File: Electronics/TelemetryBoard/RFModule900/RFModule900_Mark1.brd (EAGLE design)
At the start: 100 x 80 mm, 134 parts, among them T1 DC08-73, T2 DC08-73, U1 TPS2561, U2 TPS2561, U3 LM75B, U4 LTC5505, U5 LTC5505, U6 MCP4728, U7 ADC128D818, U8 MIC5504-3.3YM5, Y1 30 Mhz

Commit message: wiring up new buck and 3.3v ldo
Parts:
- removed JP2, JP3: (no value), SparkFun-Connectors:AVR_ICSP
- added C18, C57, C61: 100uF, SparkFun-Retired:1206
- added C48, C58: 100uF, RitLaunchInitiative:CERAMIC_CAP_1210
- added C59: 47uF, RitLaunchInitiative:CERAMIC_CAP_1210
- added C60, C64, C66: 0.1uF, SparkFun-Capacitors:0402-CAP
- added C62, C63, C65: 1uF, SparkFun-Capacitors:0402-CAP
- added D1, D2: (no value), SparkFun-LED:LED-0603
- added R29: 287, SparkFun-Resistors:0402-RES
- added R30: 90.9k, SparkFun-Resistors:0402-RES
- added R31, R32, R33: 270, SparkFun-Resistors:0402-RES
- added R34, R35: 5k, SparkFun-Resistors:0402-RES
- C32: value 1uF -> DNP
- C54: value 0.1uF -> DNP
- D3: value (none) -> DNP
- R11: value 220 -> DNP
- moved U8 411.2 mm to (12.7, 68.6)
- moved U7 393.7 mm to (31.8, 55.9)
- moved U$15 349.0 mm to (29.2, 8.89)
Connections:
- new net 12V: C48.P$1, C58.P$1, C59.P$1, C60.1, U$15.P$1, U$15.P$11, U$15.P$12, U$15.P$3, U$15.P$39, U$15.P$40
- new net 3V6_PWRGD: U$15.P$8
- new net ADC_INT: U7.6
- new net N$54: R29.2, U$15.P$26
- new net N$55: R30.2, U$15.P$22
- new net N$56: D2.C, R32.2
- new net N$57: R33.2, U8.3
- new net N$58: D1.C, R31.2
- new net N$59: R35.2, U7.8
- new net N$60: R34.2, U7.7
- net 3.3V: now also C63.1, C65.1, C66.1, D2.A, U7.5, U8.5
- net 3.6V: now also C18.1, C57.1, C61.1, C62.2, C64.1, D1.A, R33.1, U$15.P$27, U$15.P$34, U$15.P$35, U$15.P$36, U$15.P$37, U$15.P$38, U$15.P$41, U8.1
- net GND: now also C18.2, C48.P$2, C57.2, C58.P$2, C59.P$2, C60.2, C61.2, C62.1, C63.2, C64.2, C65.2, C66.2, R29.1, R30.1, R31.1, R32.1, R34.1, R35.1, U$15.P$2, U$15.P$20, U$15.P$21, U$15.P$23, U$15.P$31, U$15.P$32, U$15.P$33, U7.4, U8.2
- net SCL: now also U7.3
- net SDA: now also U7.2

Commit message: continued work
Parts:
- added R36, R37, R38: 5k, SparkFun-Resistors:0402-RES
- added R39: DNP, SparkFun-Resistors:0402-RES
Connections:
- new net N$61: R36.2, U3.P$5
- new net N$62: R37.2, U3.P$6
- new net N$63: R38.2, U3.P$7
- new net N$64: R39.2, U6.P$4
- new net PA_OVERTEMP_ALARM: U3.P$3
- net GND: now also R36.1, R37.1, R38.1, R39.1; no longer U6.P$4
- net PA_PWR_REF: now also U7.14
- net PA_PWR_SENSE: now also U7.13
- net PA_TEMP: now also U7.12
- net RF_POWER_IN: now also U7.16
- net RF_POWER_OUT: now also U7.15
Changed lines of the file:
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@@
 <element name="R34" library="SparkFun-Resistors" package="0402-RES" value="5k" x="-95.25" y="-407.67"/>
 <element name="R35" library="SparkFun-Resistors" package="0402-RES" value="5k" x="-95.25" y="-411.48"/>
+<element name="R36" library="SparkFun-Resistors" package="0402-RES" value="5k" x="-95.25" y="-415.29"/>
+<element name="R37" library="SparkFun-Resistors" package="0402-RES" value="5k" x="-95.25" y="-419.1"/>
+<element name="R38" library="SparkFun-Resistors" package="0402-RES" value="5k" x="-95.25" y="-422.91"/>
+<element name="R39" library="SparkFun-Resistors" package="0402-RES" value="DNP" x="-95.25" y="-426.72"/>
 </elements>
 <signals>
@@
 <contactref element="C49" pad="C"/>
 <contactref element="C50" pad="C"/>
-<contactref element="U6" pad="P$4"/>
 <contactref element="C11" pad="2"/>
 <contactref element="C17" pad="1"/>
@@
 <contactref element="R34" pad="1"/>
 <contactref element="R35" pad="1"/>
+<contactref element="R36" pad="1"/>
+<contactref element="R37" pad="1"/>
+<contactref element="R38" pad="1"/>
+<contactref element="R39" pad="1"/>
 <wire x1="-95.83" y1="-407.67" x2="-95.83" y2="-411.48" width="0" layer="19" extent="1-1"/>
+<wire x1="-95.83" y1="-415.29" x2="-95.83" y2="-411.48" width="0" layer="19" extent="1-1"/>
+<wire x1="-95.83" y1="-419.1" x2="-95.83" y2="-415.29" width="0" layer="19" extent="1-1"/>
+<wire x1="-95.83" y1="-422.91" x2="-95.83" y2="-419.1" width="0" layer="19" extent="1-1"/>
+<wire x1="-95.83" y1="-426.72" x2="-95.83" y2="-422.91" width="0" layer="19" extent="1-1"/>
 <wire x1="-94.67" y1="-403.86" x2="-95.83" y2="-407.67" width="0" layer="19" extent="1-1"/>
 <wire x1="-94.67" y1="-400.05" x2="-94.67" y2="-403.86" width="0" layer="19" extent="1-1"/>
@@
 <wire x1="11.3999" y1="68.58" x2="-18.47" y2="55.88" width="0" layer="19" extent="1-1"/>
 <wire x1="31.425" y1="52.91" x2="11.3999" y2="68.58" width="0" layer="19" extent="1-1"/>
-<wire x1="36.125" y1="47.76" x2="31.425" y2="52.91" width="0" layer="19" extent="1-1"/>
+<wire x1="40.075" y1="49.26" x2="31.425" y2="52.91" width="0" layer="19" extent="1-1"/>
 <wire x1="100.8634" y1="19.6479" x2="100.8634" y2="19.6479" width="0" layer="19" extent="1-16"/>
 <wire x1="100.8634" y1="10.8829" x2="100.8634" y2="10.8829" width="0" layer="19" extent="1-16"/>
@@
 <contactref element="U5" pad="P$4"/>
 <contactref element="U$6" pad="3"/>
+<contactref element="U7" pad="16"/>
+<wire x1="29.475" y1="58.85" x2="68.9" y2="63.5301" width="0" layer="19" extent="1-1"/>
 <wire x1="93.03" y1="1.721" x2="68.9" y2="63.5301" width="0" layer="19" extent="1-1"/>
 </signal>
 <signal name="RF_POWER_OUT">
 <contactref element="U4" pad="P$4"/>
+<contactref element="U7" pad="15"/>
+<wire x1="30.125" y1="58.85" x2="92.0725" y2="26.219" width="0" layer="19" extent="1-1"/>
 </signal>
 <signal name="N$38">
@@
 <contactref element="R14" pad="1"/>
 <contactref element="R13" pad="2"/>
+<contactref element="U7" pad="13"/>
 <wire x1="-87.05" y1="-281.94" x2="-88.21" y2="-285.75" width="0" layer="19" extent="1-1"/>
+<wire x1="31.425" y1="58.85" x2="-87.05" y2="-281.94" width="0" layer="19" extent="1-1"/>
 </signal>
 <signal name="PA_PWR_REF">
 <contactref element="R21" pad="1"/>
 <contactref element="R20" pad="2"/>
+<contactref element="U7" pad="14"/>
 <wire x1="-87.05" y1="-289.56" x2="-88.21" y2="-293.37" width="0" layer="19" extent="1-1"/>
+<wire x1="30.775" y1="58.85" x2="-87.05" y2="-289.56" width="0" layer="19" extent="1-1"/>
 </signal>
 <signal name="PA_TEMP">
 <contactref element="R28" pad="1"/>
 <contactref element="U$16" pad="1"/>
+<contactref element="U7" pad="12"/>
 <wire x1="-88.21" y1="-311.15" x2="-88.21" y2="-313.69" width="0" layer="19" extent="1-1"/>
+<wire x1="32.075" y1="58.85" x2="-88.21" y2="-311.15" width="0" layer="19" extent="1-1"/>
 </signal>
 <signal name="N$54">
@@
 <wire x1="33.375" y1="52.91" x2="-94.67" y2="-407.67" width="0" layer="19" extent="1-1"/>
 </signal>
+<signal name="N$61">
+<contactref element="U3" pad="P$5"/>
+<contactref element="R36" pad="2"/>
+<wire x1="-94.67" y1="-415.29" x2="-86.2175" y2="-278.88" width="0" layer="19" extent="1-1"/>
+</signal>
+<signal name="N$62">
+<contactref element="U3" pad="P$6"/>
+<contactref element="R37" pad="2"/>
+<wire x1="-94.67" y1="-419.1" x2="-86.2175" y2="-278.38" width="0" layer="19" extent="1-1"/>
+</signal>
+<signal name="N$63">
+<contactref element="U3" pad="P$7"/>
+<contactref element="R38" pad="2"/>
+<wire x1="-94.67" y1="-422.91" x2="-86.2175" y2="-277.88" width="0" layer="19" extent="1-1"/>
+</signal>
+<signal name="PA_OVERTEMP_ALARM">
+<contactref element="U3" pad="P$3"/>
+</signal>
+<signal name="N$64">
+<contactref element="U6" pad="P$4"/>
+<contactref element="R39" pad="2"/>
+<wire x1="-94.67" y1="-426.72" x2="36.125" y2="47.76" width="0" layer="19" extent="1-1"/>
+</signal>
 </signals>

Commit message: Added TVS array and diode
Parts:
- removed JP1: (no value), SparkFun-Connectors:2X10_LOCK_SPECIAL
- removed JP4: (no value), SparkFun-Connectors:1X01
- added D10, D11, D12, D13, D7: PESD5V0U5BF, RitLaunchInitiative:6-XFDFN
- added R40, R41: 10k, SparkFun-Resistors:0402-RES
- added U$12: DFLT13A-7, RitLaunchInitiative:POWERDI®123
- added U$20, U$21: 10k, RitLaunchInitiative:0402
- added X1: 679105700, con-molex:679105700
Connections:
- new net BUCK_TEMP: R40.1, U$20.1, U7.11
- new net PA_LOADSWITCH_TEMP: R41.1, U$21.1, U7.10
- net 12V: now also U$12.CATHODE
- net 3.3V: now also R40.2, R41.2; no longer JP1.1, JP1.2, JP1.3, JP1.4, JP1.6
- net 3V6_PWRGD: now also D10.P$5
- net 5V: no longer JP1.9
- net BUFF_TR_SWITCH_CTL: now also D12.P$6
- net DAC_PWR_EN: now also D7.P$1
- net DAC_PWR_FAULT: now also D10.P$1
- net GND: now also D10.P$2, D11.P$2, D12.P$2, D13.P$2, D7.P$2, U$12.ANODE, U$20.2, U$21.2; no longer JP1.10, JP1.12, JP1.5, JP1.7, JP1.8
- net N$18: now also U7.9; no longer JP4.1
- net N_IRQ: now also D11.P$4
- net N_SEL: now also D11.P$1
- net PA_BREAKER_OVERRIDE: now also D7.P$4
- net PA_PWR_EN: now also D7.P$3
- net PA_PWR_EN_BREAKER: now also D7.P$5
- net PA_PWR_FAULT: now also D10.P$4
- net PA_PWR_REF: now also D12.P$5
- net PA_PWR_SENSE: now also D12.P$4
- net PA_TEMP: now also D13.P$6
- net RADIO_PWR_EN: now also D7.P$6
- net RADIO_PWR_FAULT: now also D10.P$6
- net RADIO_SHUTDOWN: now also D10.P$3
- net RF_POWER_IN: now also D12.P$1
- net RF_POWER_OUT: now also D12.P$3
- net SCL: now also D13.P$1
- net SCLK: now also D11.P$5
- net SDA: now also D13.P$3
- net SDI: now also D11.P$6
- net SDO: now also D11.P$3
- net VSWR_BREAKER_STATE: now also D13.P$5

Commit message: finishing card edge connector
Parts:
- removed X1: 679105700, con-molex:679105700
- added U$13: RADIO_HEAD_EDGECONNECTOR, RitLaunchInitiative:PCIE_MINI_CARDEDGE
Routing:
- removed copper zone on layer 1, net GND
- removed copper zone on layer 16, net GND
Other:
- board size 100 x 80 mm -> 100 x 30 mm
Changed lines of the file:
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@@
 <board>
 <plain>
-<wire x1="0" y1="0" x2="100" y2="0" width="0" layer="20"/>
-<wire x1="100" y1="0" x2="100" y2="80" width="0" layer="20"/>
-<wire x1="100" y1="80" x2="0" y2="80" width="0" layer="20"/>
-<wire x1="0" y1="80" x2="0" y2="0" width="0" layer="20"/>
 </plain>
 <attributes>
@@
 <element name="R38" library="SparkFun-Resistors" package="0402-RES" value="5k" x="-95.25" y="-422.91"/>
 <element name="R39" library="SparkFun-Resistors" package="0402-RES" value="DNP" x="-95.25" y="-426.72"/>
-<element name="X1" library="con-molex" package="679105700" value="679105700" x="-127" y="-422.91">
-<attribute name="OC_NEWARK" value="93M2128" x="-127" y="-422.91" size="1.778" layer="27" display="off"/>
-<attribute name="MPN" value="67910-5700" x="-127" y="-422.91" size="1.778" layer="27" display="off"/>
-<attribute name="MF" value="" x="-127" y="-422.91" size="1.778" layer="27" display="off"/>
-<attribute name="OC_FARNELL" value="unknown" x="-127" y="-422.91" size="1.778" layer="27" display="off"/>
-</element>
 <element name="D7" library="RitLaunchInitiative" package="6-XFDFN" value="PESD5V0U5BF" x="-128.27" y="-430.53">
 <attribute name="DIGI" value="568-7355-1-ND" x="-128.27" y="-430.53" size="1.778" layer="27" display="off"/>
@@
 <attribute name="MPN" value="DFLT13A-7" x="-125.73" y="-473.71" size="1.778" layer="27" display="off"/>
 </element>
+<element name="U$13" library="RitLaunchInitiative" package="PCIE_MINI_CARDEDGE" value="RADIO_HEAD_EDGECONNECTOR" x="0" y="15.24" rot="R180"/>
 </elements>
 <signals>
@@
 <contactref element="U$10" pad="GND@2"/>
 <contactref element="U$10" pad="GND@1"/>
-<polygon width="0.4064" layer="16" thermals="no">
-<vertex x="0" y="0"/>
-<vertex x="0" y="80.01"/>
-<vertex x="38.1" y="80.01"/>
-<vertex x="38.1" y="0"/>
-</polygon>
-<polygon width="0.4064" layer="1" thermals="no">
-<vertex x="0" y="0"/>
-<vertex x="0" y="83.82"/>
-<vertex x="99.06" y="83.82"/>
-<vertex x="99.06" y="0"/>
-</polygon>
 <contactref element="U5" pad="P$2"/>
 <contactref element="C49" pad="C"/>

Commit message: added TCA9535 IO expander to simplify API if needed
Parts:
- removed C54: DNP, SparkFun-Capacitors:0402-CAP
- removed D12: PESD5V0U5BF, RitLaunchInitiative:6-XFDFN
- removed D3: DNP, SparkFun-LED:LED-0603
- removed U$4: LP3984_DNP, RitLaunchInitiative:SOT23-5
- added R42, R43: 5k, SparkFun-Resistors:0402-RES
- added SJ6: JUMPER-PAD-2-NOYES_SILK, SparkFun-Passives:PAD-JUMPER-2-NO_YES_SILK
- added U9: TCA9535, RitLaunchInitiative:24-VFQFN
- C32: value DNP -> 0.1uF; device SparkFun-Capacitors:EIA3216 -> SparkFun-Capacitors:0402-CAP
- R11: value DNP -> 5k
- moved U$12 591.8 mm to (86.4, 78.7), turned to 90 degrees
- moved D13 573.9 mm to (73.7, 76.2), turned to 90 degrees
- moved U$21 569.0 mm to (69.8, 76.2), turned to 90 degrees
- moved R41 564.1 mm to (66.0, 76.2), turned to 90 degrees
- moved U$20 559.2 mm to (62.2, 76.2), turned to 90 degrees
- moved R40 554.4 mm to (58.4, 76.2), turned to 90 degrees
- moved D11 544.6 mm to (50.8, 76.2), turned to 90 degrees
- moved D10 539.8 mm to (47.0, 76.2), turned to 90 degrees
- moved D7 534.9 mm to (43.2, 76.2), turned to 90 degrees
- moved R39 515.0 mm to (45.7, 68.6), turned to 90 degrees
- moved R38 510.3 mm to (41.9, 68.6), turned to 90 degrees
- moved R37 505.6 mm to (38.1, 68.6), turned to 90 degrees
- moved R36 500.9 mm to (34.3, 68.6), turned to 90 degrees
- moved R35 496.3 mm to (30.5, 68.6), turned to 90 degrees
- moved R34 491.6 mm to (26.7, 68.6), turned to 90 degrees
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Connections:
- new net EXPANDER_IRQ: U$13.P$9, U9.P$22
- new net N$66: R11.2, U9.P$18
- new net N$67: R42.2, U9.P$23
- new net N$68: R43.2, U9.P$24
- net 12V: now also U$13.P$45, U$13.P$47, U$13.P$49, U$13.P$51
- net 3.3V: now also C32.1, SJ6.2, U9.P$21
- net 3V1: no longer C32.A, D3.A, U$4.5
- net 3V6_PWRGD: now also U$13.P$18, U9.P$7
- net 5V: no longer C54.2, U$4.1
- net BUFF_TR_SWITCH_CTL: now also D13.P$6, U$13.P$25, U9.P$5; no longer D12.P$6
- net DAC_PWR_EN: now also U$13.P$10, U9.P$17
- net DAC_PWR_FAULT: now also U$13.P$24, U9.P$11
- net GND: now also C32.2, R42.1, R43.1, U$13.P$11, U$13.P$12, U$13.P$15, U$13.P$16, U$13.P$22, U$13.P$27, U$13.P$28, U$13.P$3, U$13.P$30, U$13.P$34, U$13.P$38, U$13.P$4, U$13.P$42, U$13.P$44, U$13.P$46, U$13.P$48, U$13.P$7, U$13.P$8, U9.P$9, U9.P$GND_PAD; no longer C32.C, C54.1, D12.P$2, U$4.2
- net N$7: now also SJ6.1, U$13.P$29, U$13.P$31, U$13.P$33, U$13.P$35, U$13.P$37, U$13.P$39; no longer D3.C, R11.2
- net N_IRQ: now also U$13.P$32
- net N_SEL: now also U$13.P$6
- net PA_BREAKER_OVERRIDE: now also U$13.P$17, U9.P$14
- net PA_PWR_EN: now also U$13.P$14, U9.P$15
- net PA_PWR_EN_BREAKER: now also U$13.P$19, U9.P$13; no longer U$4.3
- net PA_PWR_FAULT: now also U$13.P$20, U9.P$8
- net PA_PWR_REF: no longer D12.P$5
- net PA_PWR_SENSE: no longer D12.P$4
- net PA_TEMP: no longer D13.P$6
- net RADIO_PWR_EN: now also U$13.P$13, U9.P$16
- net RADIO_PWR_FAULT: now also U$13.P$26, U9.P$10
- net RADIO_SHUTDOWN: now also U$13.P$23, U9.P$6
- net RF_POWER_IN: no longer D12.P$1
- net RF_POWER_OUT: no longer D12.P$3
- net SCL: now also U$13.P$40, U9.P$19
- net SCLK: now also U$13.P$2
- net SDA: now also U$13.P$36, U9.P$20
- net SDI: now also U$13.P$1
- net SDO: now also U$13.P$5
- net VSWR_BREAKER_STATE: now also U$13.P$21, U9.P$12
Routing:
- added copper zone on layer 16, net N$3

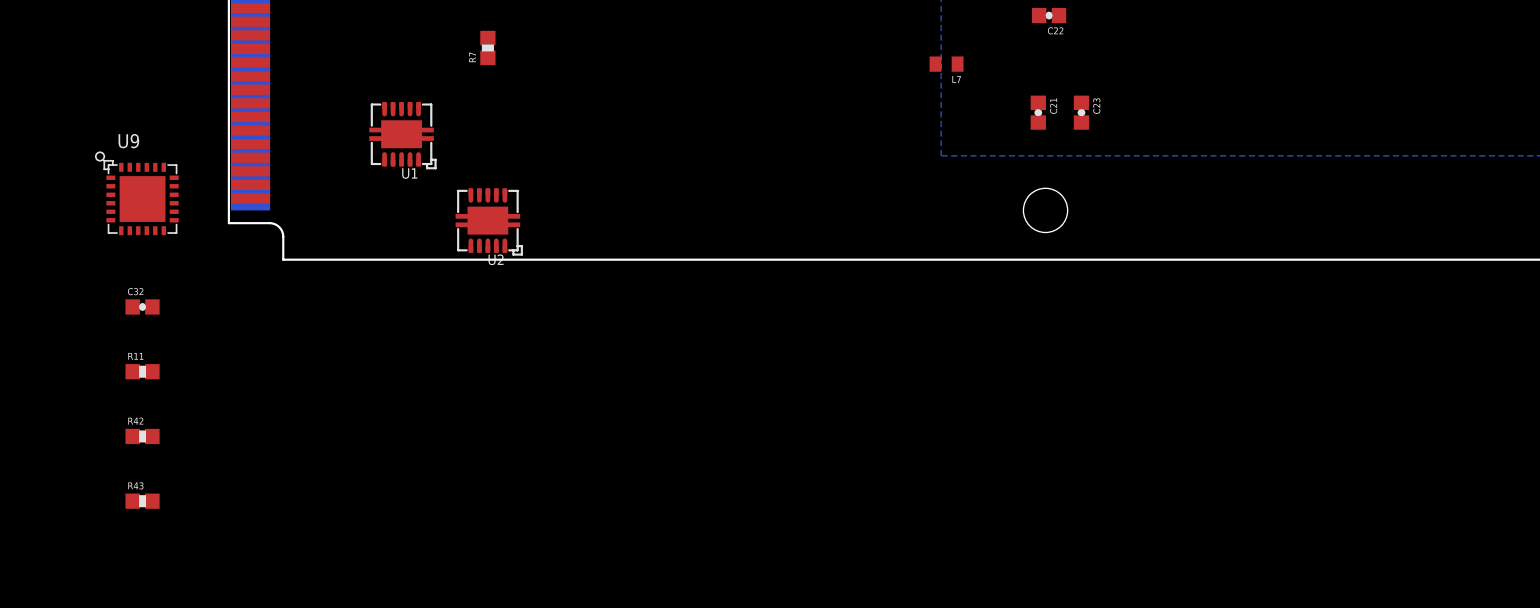
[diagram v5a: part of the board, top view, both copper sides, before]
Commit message: Fixed package on new IO expander
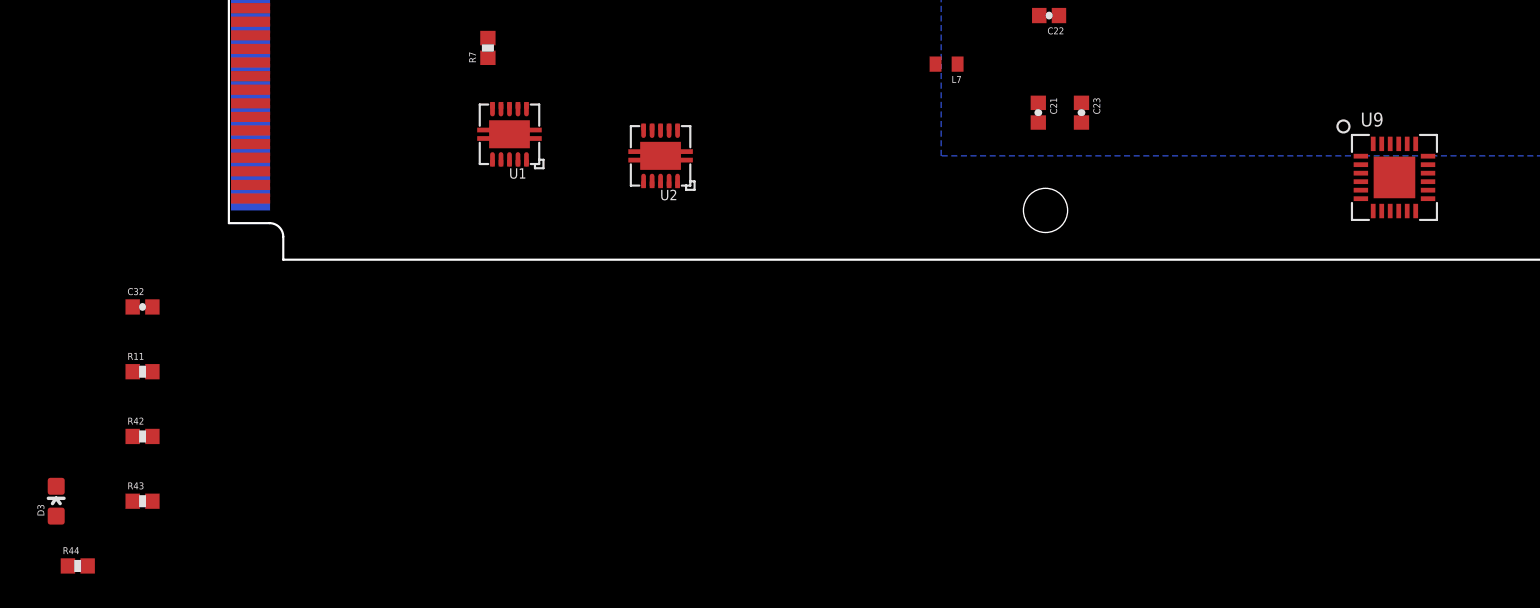
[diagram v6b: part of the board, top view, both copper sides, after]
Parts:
- added D3: (no value), SparkFun-LED:LED-0603
- added R44: 270, SparkFun-Resistors:0402-RES
- U9: device RitLaunchInitiative:24-VFQFN -> RitLaunchInitiative:24-WQFN
- moved U9 73.7 mm to (68.6, 5.08)
- moved U2 10.9 mm to (25.4, 6.35)
- moved U1 6.35 mm to (16.5, 7.62)
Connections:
- new net N$65: D3.A, U9.P$1
- net GND: now also U9.GND_PAD; no longer U9.P$GND_PAD
- net PA_OVERTEMP_ALARM: now also D13.P$4, U$13.P$52, U9.P$4
